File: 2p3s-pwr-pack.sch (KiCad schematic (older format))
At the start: 23 parts, among them P1 PAD, P10 PAD, P11 PAD, P12 PAD, P13 Conn_Basic_2_pin, P14 PAD, P15 PAD, P16 Conn_Basic_2_pin, P2 PAD, P3 PAD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

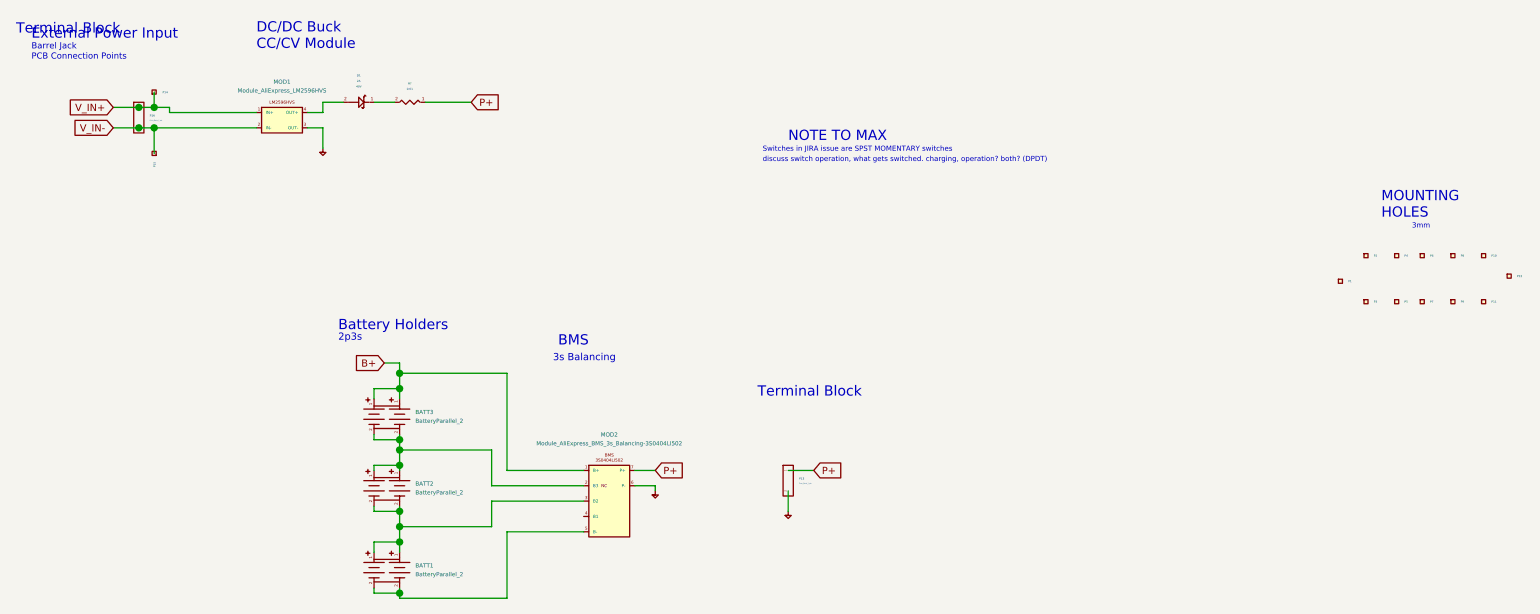
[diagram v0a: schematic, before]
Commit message: remove hole in the way
battery mounting clip in the middle interfered with enclosure stantion boss. removed the battery mounting clip
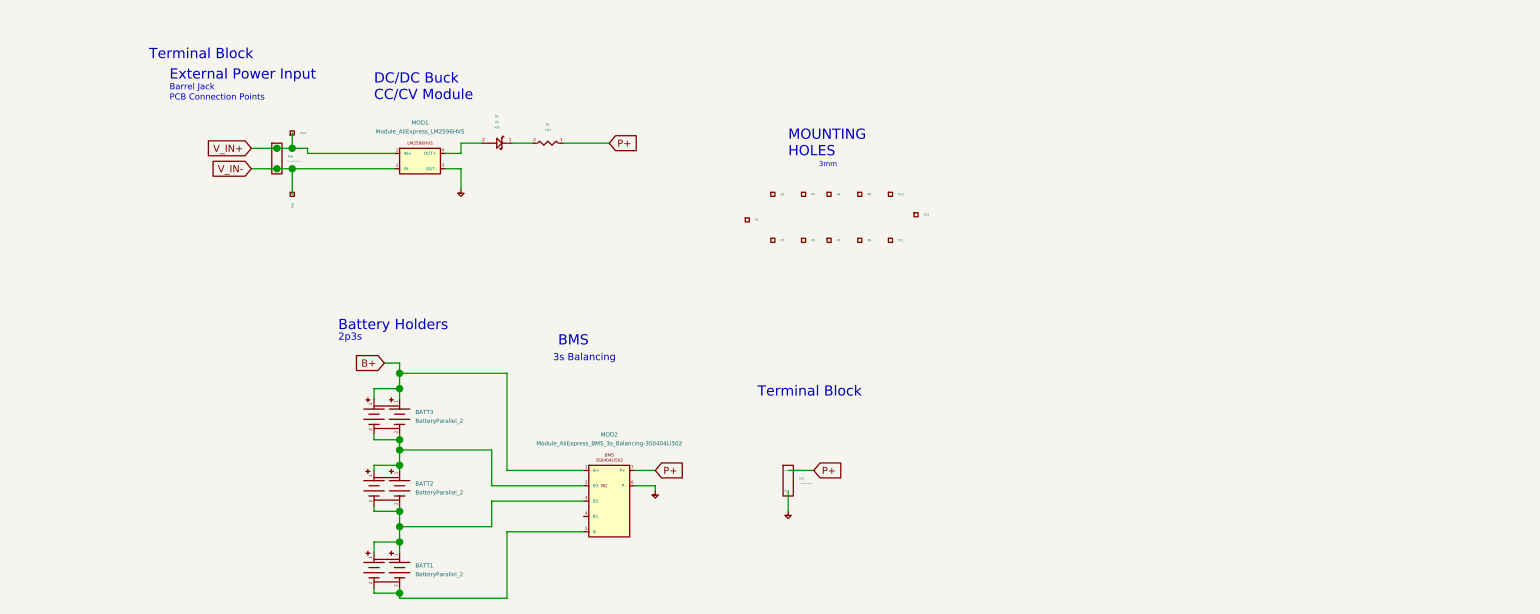
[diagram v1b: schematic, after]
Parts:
- gave numbers to parts that had none: 1
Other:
- note removed: "NOTE TO MAX"
- note removed: "Switches in JIRA issue are SPST MOMENTARY switches"
- note removed: "discuss switch operation, what gets switched. charging, operation? both? (DPDT)"
- moved on the sheet: D1, MOD1, P1, P10, P11, P12, P14, P15, P16, P2, P3, P4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

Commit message: KiCAD design files as in 3May2019 gerber files
These are the KICAD design files that the may3 gerber outputs were produced from.
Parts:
- added P17, P19: PAD, NPTH_3mm, symbol __SimpleParts:PAD
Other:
- note added: "Battery \nTie-Down\nHoles"
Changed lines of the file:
@@
 Wire Wire Line
 	3700 3425 3925 3425
+$Comp
+L __SimpleParts:PAD P17
+U 1 1 5CC9F4D9
+P 2000 5000
+F 0 "P17" H 2038 5000 10  0000 L CNN
+F 1 "PAD" H 2000 5000 3   0001 C CNN
+F 2 "NPTH_3mm" H 1900 4925 60  0001 C CNN
+F 3 "" H 2030 5000 60  0001 C CNN
+F 4 "MFG1" H 2000 4975 6   0001 C CNN "Manufacturer1"
+F 5 "MFG1PN" H 2000 5000 6   0001 C CNN "Manufacturer1PartNumber"
+	1    2000 5000
+	1    0    0    -1
+$EndComp
+Text Notes 1925 4900 0    50   ~ 0
+Battery \nTie-Down\nHoles
+$Comp
+L __SimpleParts:PAD P19
+U 1 1 5CCA29D3
+P 2200 5000
+F 0 "P19" H 2238 5000 10  0000 L CNN
+F 1 "PAD" H 2200 5000 3   0001 C CNN
+F 2 "NPTH_3mm" H 2100 4925 60  0001 C CNN
+F 3 "" H 2230 5000 60  0001 C CNN
+F 4 "MFG1" H 2200 4975 6   0001 C CNN "Manufacturer1"
+F 5 "MFG1PN" H 2200 5000 6   0001 C CNN "Manufacturer1PartNumber"
+	1    2200 5000
+	1    0    0    -1
+$EndComp
 $EndSCHEMATC
